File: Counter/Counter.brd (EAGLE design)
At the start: 68.6 x 72.1 mm, 6 parts

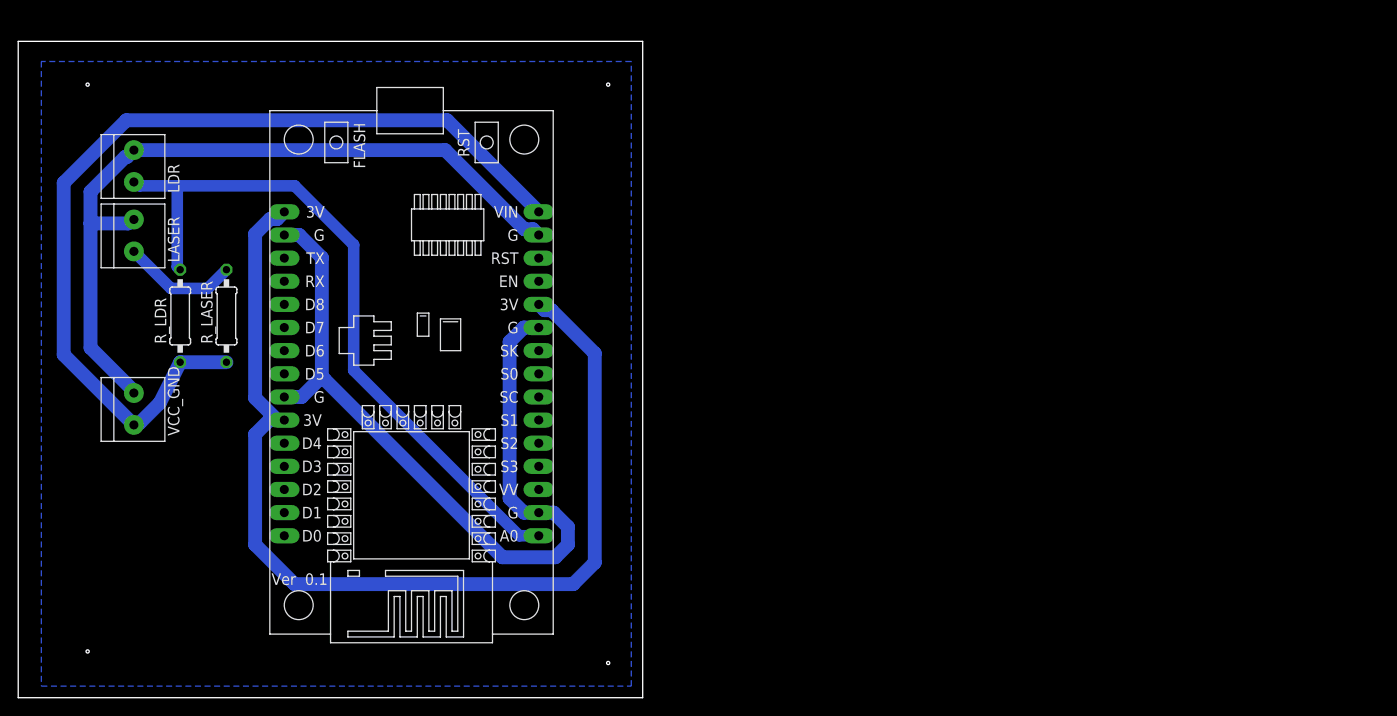
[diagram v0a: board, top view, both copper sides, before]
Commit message: revisi rangkaian rev 3 + penambahan reset
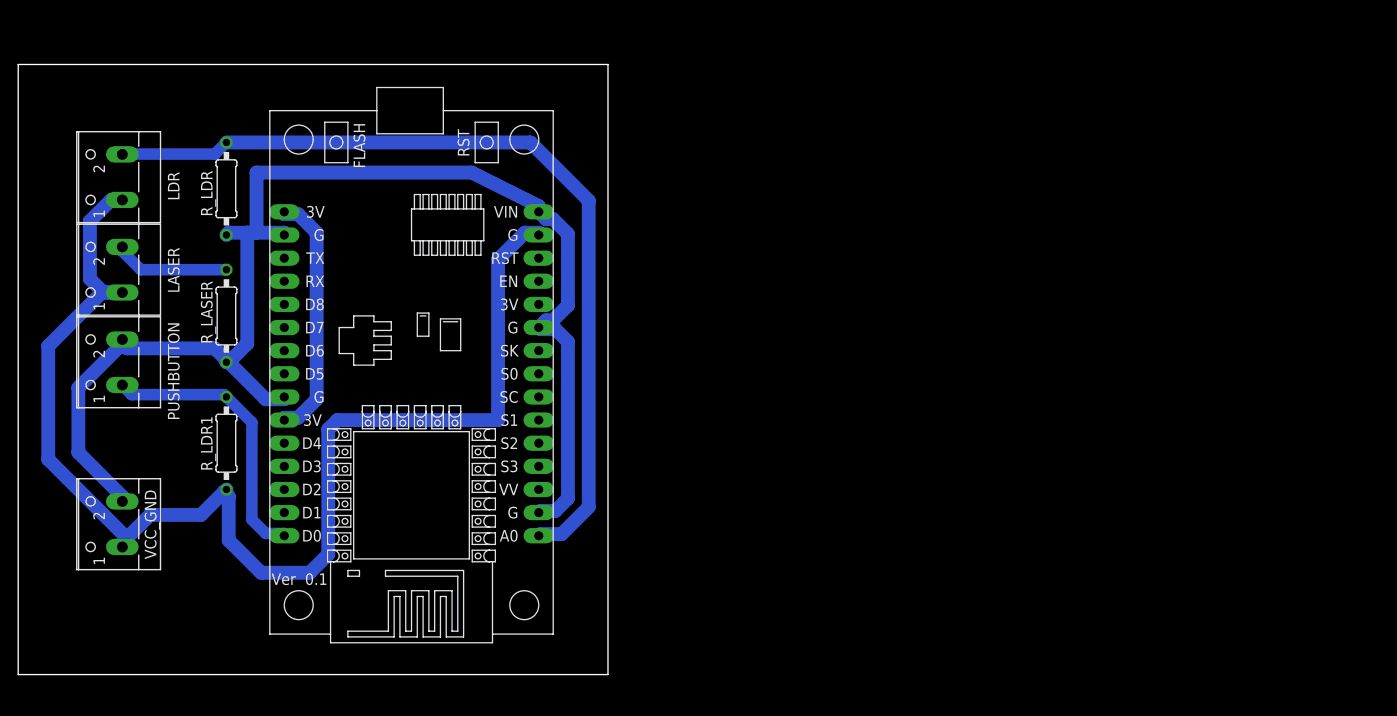
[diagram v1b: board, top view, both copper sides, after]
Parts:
- added PUSHBUTTON: (no value), con-wago-500:W237-102
- added R_LDR1: 10k, rcl:0207/10
- LASER, LDR, VCC_GND: value 1X2-3.5MM -> (none); device adafruit:1X2-3.5MM -> con-wago-500:W237-102
- moved R_LDR 14.9 mm to (34.3, 82.5)
- moved VCC_GND 13.0 mm to (21.6, 45.7), turned to 90 degrees
- moved LASER 4.58 mm to (21.6, 73.7), turned to 90 degrees
- moved LDR 2.84 mm to (21.6, 83.8), turned to 90 degrees
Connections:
- removed net GROUND: LASER.2, LDR.2, U$1.14, VCC_GND.2
- new net N$1: LDR.2, R_LDR.2, U$1.1
- new net S$1: U$1.11
- net 3V: no longer U$1.11
- net GND: now also PUSHBUTTON.2, R_LASER.1, R_LDR.1, U$1.15, VCC_GND.2
- net N$2: now also LASER.2; no longer LASER.1
- net N$3: now also PUSHBUTTON.1, R_LDR1.2, U$1.30; no longer LDR.1, R_LDR.2, U$1.1
- net VCC: now also LASER.1, LDR.1, R_LDR1.1, U$1.14; no longer R_LASER.1, R_LDR.1, U$1.15
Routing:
- net N$1: track 0.00 -> 94.8 mm
- net 3V: track 113.8 -> 27.6 mm
- net GROUND: track 84.0 -> 0.00 mm
- net GND: track 89.8 -> 144.5 mm
- net N$3: track 78.0 -> 31.1 mm
- net VCC: track 102.8 -> 139.7 mm
- removed copper zone on layer 16, net BG
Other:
- board size 68.6 x 72.1 mm -> 64.8 x 67 mm

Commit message: penambahan fuse dan lampu indikator pada board, pembuatan masking. penambahan program counter
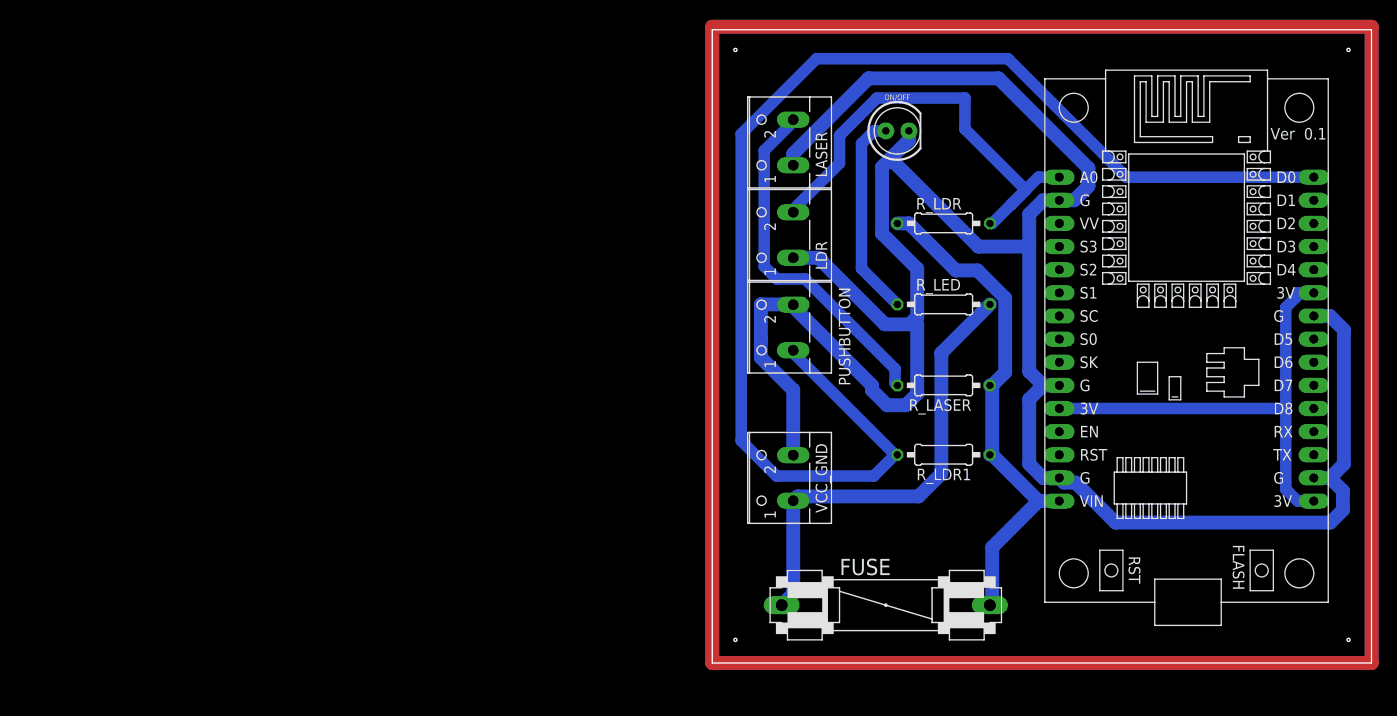
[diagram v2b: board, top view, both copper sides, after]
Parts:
- added FUSE: (no value), special:FUSE
- added ON/OFF: (no value), SparkFun-LED:LED_5MM
- added R_LED: 330, rcl:0207/10
- moved U$1 85.2 mm to (139.7, 66.0), turned to 0 degrees
- moved R_LASER 79.1 mm to (113.0, 61.0), turned to 180 degrees
- moved R_LDR 78.8 mm to (113.0, 78.7), turned to 0 degrees
- moved R_LDR1 78.8 mm to (113.0, 53.3), turned to 180 degrees
- moved LASER 75.0 mm to (95.2, 87.6)
- moved LDR 73.9 mm to (95.2, 77.5)
- moved VCC_GND 73.8 mm to (95.2, 50.8)
- moved PUSHBUTTON 73.8 mm to (95.2, 67.3)
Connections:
- removed net S$1: U$1.11
- new net N$4: FUSE.2, R_LASER.1, R_LDR.1, R_LDR1.1, U$1.15
- new net N$5: ON/OFF.A, R_LED.1
- net 3V: now also U$1.11
- net GND: now also LASER.1, LDR.1, ON/OFF.K, U$1.14; no longer R_LASER.1, R_LDR.1, U$1.15
- net VCC: now also FUSE.1, R_LED.2; no longer LASER.1, LDR.1, R_LDR1.1, U$1.14
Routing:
- net N$7: track 0.00 -> 284.5 mm
- net N$6: track 0.00 -> 284.5 mm
- net N$3: track 31.1 -> 141.2 mm
- net GND: track 144.5 -> 254.3 mm
- net VCC: track 139.7 -> 50.3 mm
- net N$4: track 0.00 -> 56.6 mm
- net N$1: track 94.8 -> 50.9 mm
- net N$2: track 12.7 -> 38.4 mm
- net 3V: track 27.6 -> 52.4 mm
- net N$5: track 0.00 -> 22.5 mm
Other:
- board size 64.8 x 67 mm -> 72.4 x 69.5 mm

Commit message: penambahan reset counter
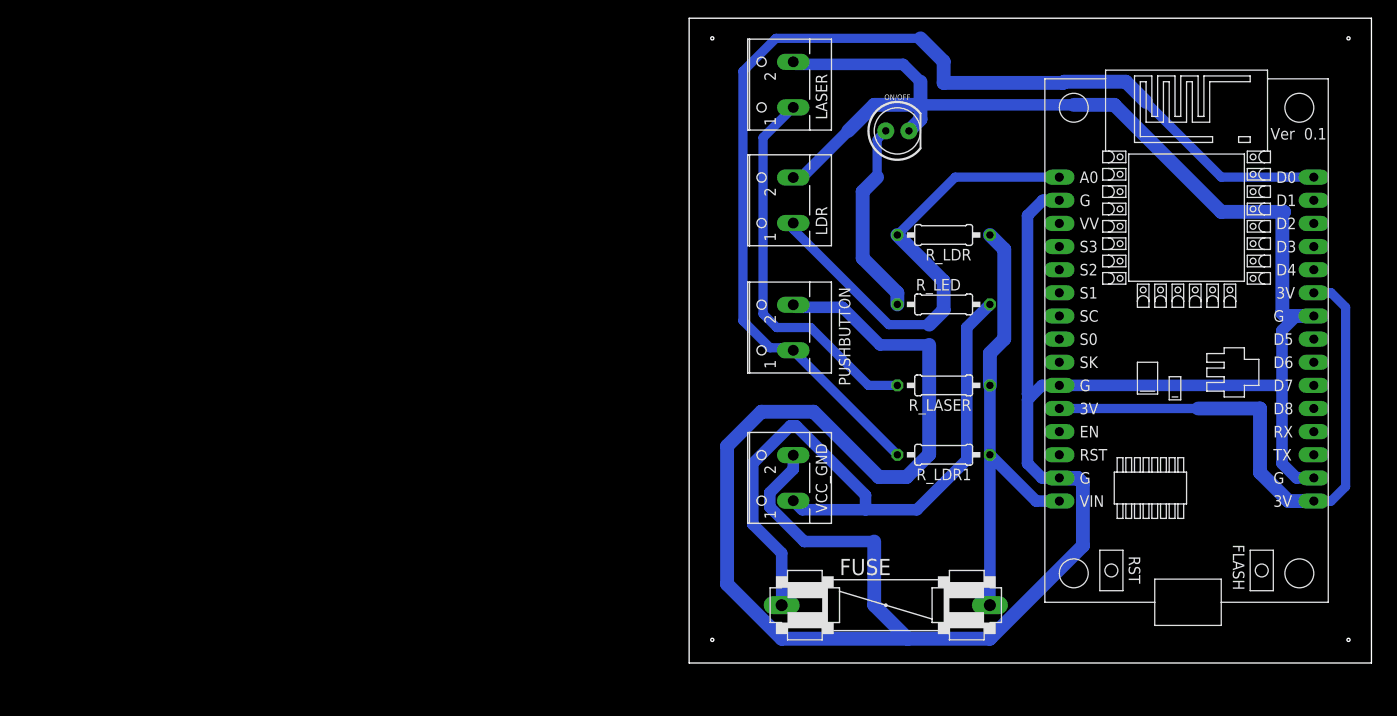
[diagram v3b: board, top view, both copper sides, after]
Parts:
- FUSE: value (none) -> 1 AMP
- ON/OFF: value (none) -> GREEN
- moved LASER 6.35 mm to (95.2, 94.0)
- moved LDR 3.81 mm to (95.2, 81.3)
- moved R_LDR 1.27 mm to (113.0, 77.5), turned to 180 degrees
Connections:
- net GND: now also LASER.2, LDR.2; no longer LASER.1, LDR.1
- net N$1: now also LDR.1; no longer LDR.2
- net N$2: now also LASER.1; no longer LASER.2
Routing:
- net N$7: track 284.5 -> 0.00 mm
- net N$6: track 284.5 -> 0.00 mm
- net GND: track 254.3 -> 345.7 mm
- net VCC: track 50.3 -> 75.6 mm
- net N$3: track 141.2 -> 122.4 mm
- net 3V: track 52.4 -> 64.3 mm
- net N$9: track 56.6 -> 51.7 mm
- net N$2: track 38.4 -> 42.0 mm
- net N$1: track 50.9 -> 53.0 mm
- net N$5: track 22.5 -> 21.7 mm
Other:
- board size 72.4 x 69.5 mm -> 74.9 x 70.8 mm
